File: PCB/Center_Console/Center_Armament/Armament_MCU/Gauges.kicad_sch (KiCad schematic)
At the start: 4 parts, among them U5 DRV8833PW

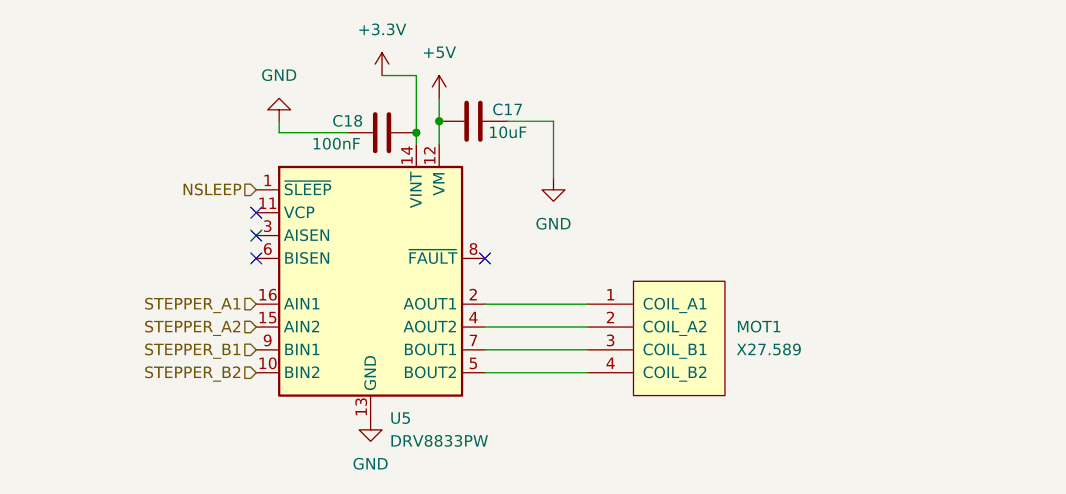
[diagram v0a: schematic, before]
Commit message: Switch stepper driver DRV8835 → DRV8833PW; rework IRLML2502 symbol
DRV8835 is only available in WSON-12 (bottom-terminated, not inspectable
post-reflow). Replaced throughout with DRV8833PW (HTSSOP-16) which is
already placed in Gauges.kicad_sch as the placeholder.

Library: remove DRV8835 symbol block from OpenSkyhawk.kicad_sym; rework
IRLML2502 symbol body with proper N-channel MOSFET graphical elements
(was a plain rectangle).

Docs: update hardware-standards.md stepper driver section (DRV8833PW,
VINT/VCP/AISEN/FAULT handling); update kicad.md library table; update
Center_Armament.md MCU board component list.

Schematics: KiCad project file and sub-sheets updated from Symbol Editor
session (IRLML2502 symbol refresh across Backlighting and Gauges sheets).
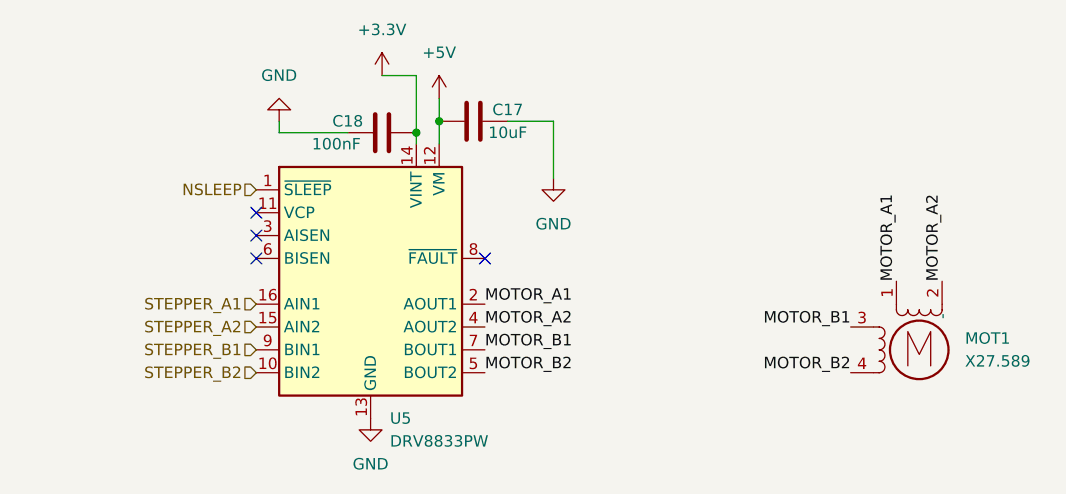
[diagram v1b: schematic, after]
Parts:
- C17, C18: footprint (none) -> Capacitor_SMD:C_0805_2012Metric
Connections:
- net MOTOR_A1: now reaches MOT1.1, U5.2 (AOUT1)
- net MOTOR_A2: now reaches MOT1.2 (-), U5.4 (AOUT2)
- net MOTOR_B1: now reaches MOT1.3, U5.7 (BOUT1)
- net MOTOR_B2: now reaches MOT1.4, U5.5 (BOUT2)
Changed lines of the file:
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@@
 	(wire
 		(pts
-			(xy 194.31 74.93) (xy 205.74 74.93)
+			(xy 196.85 54.61) (xy 201.93 54.61)
 		)
 		(stroke
@@
 	(wire
 		(pts
-			(xy 196.85 54.61) (xy 201.93 54.61)
+			(xy 186.69 57.15) (xy 186.69 55.88)
 		)
 		(stroke
@@
 	(wire
 		(pts
-			(xy 186.69 57.15) (xy 186.69 55.88)
+			(xy 189.23 52.07) (xy 189.23 54.61)
 		)
 		(stroke
@@
 	(wire
 		(pts
-			(xy 189.23 52.07) (xy 189.23 54.61)
+			(xy 186.69 49.53) (xy 186.69 55.88)
 		)
 		(stroke
@@
 	(wire
 		(pts
-			(xy 194.31 82.55) (xy 205.74 82.55)
+			(xy 201.93 54.61) (xy 201.93 60.96)
 		)
 		(stroke
@@
 	(wire
 		(pts
-			(xy 186.69 49.53) (xy 186.69 55.88)
+			(xy 189.23 54.61) (xy 189.23 57.15)
 		)
 		(stroke
@@
 	(wire
 		(pts
-			(xy 201.93 54.61) (xy 201.93 60.96)
+			(xy 171.45 55.88) (xy 179.07 55.88)
 		)
 		(stroke
@@
 	(wire
 		(pts
-			(xy 194.31 77.47) (xy 205.74 77.47)
+			(xy 186.69 49.53) (xy 182.88 49.53)
 		)
 		(stroke
@@
 	(wire
 		(pts
-			(xy 189.23 54.61) (xy 189.23 57.15)
+			(xy 171.45 54.61) (xy 171.45 55.88)
 		)
 		(stroke
@@
 		)
 	)
-	(wire
-		(pts
-			(xy 171.45 55.88) (xy 179.07 55.88)
-		)
-		(stroke
-			(width 0)
-			(type default)
-		)
-	)
-	(wire
-		(pts
-			(xy 186.69 49.53) (xy 182.88 49.53)
-		)
-		(stroke
-			(width 0)
-			(type default)
-		)
-	)
-	(wire
-		(pts
-			(xy 171.45 54.61) (xy 171.45 55.88)
-		)
-		(stroke
-			(width 0)
-			(type default)
-		)
-	)
-	(wire
-		(pts
-			(xy 194.31 80.01) (xy 205.74 80.01)
-		)
-		(stroke
-			(width 0)
-			(type default)
+	(label "MOTOR_B1"
+		(at 194.31 80.01 0)
+		(effects
+			(font
+				(size 1.27 1.27)
+			)
+			(justify left bottom)
+		)
+	)
+	(label "MOTOR_B2"
+		(at 194.31 82.55 0)
+		(effects
+			(font
+				(size 1.27 1.27)
+			)
+			(justify left bottom)
+		)
+	)
+	(label "MOTOR_B1"
+		(at 234.95 77.47 180)
+		(effects
+			(font
+				(size 1.27 1.27)
+			)
+			(justify right bottom)
+		)
+	)
+	(label "MOTOR_A1"
+		(at 194.31 74.93 0)
+		(effects
+			(font
+				(size 1.27 1.27)
+			)
+			(justify left bottom)
+		)
+	)
+	(label "MOTOR_B2"
+		(at 234.95 82.55 180)
+		(effects
+			(font
+				(size 1.27 1.27)
+			)
+			(justify right bottom)
+		)
+	)
+	(label "MOTOR_A2"
+		(at 194.31 77.47 0)
+		(effects
+			(font
+				(size 1.27 1.27)
+			)
+			(justify left bottom)
+		)
+	)
+	(label "MOTOR_A1"
+		(at 240.03 72.39 90)
+		(effects
+			(font
+				(size 1.27 1.27)
+			)
+			(justify left bottom)
+		)
+	)
+	(label "MOTOR_A2"
+		(at 245.11 72.39 90)
+		(effects
+			(font
+				(size 1.27 1.27)
+			)
+			(justify left bottom)
 		)
 	)
@@
 			)
 		)
-		(property "Footprint" ""
+		(property "Footprint" "Capacitor_SMD:C_0805_2012Metric"
 			(at 196.85 53.6448 0)
 			(hide yes)
@@
 	(symbol
 		(lib_id "OpenSkyhawk:X27.589_Stepper")
-		(at 215.9 78.74 0)
+		(at 241.3 80.01 0)
 		(unit 1)
 		(body_style 1)
@@
 		(fields_autoplaced yes)
 		(property "Reference" "MOT1"
-			(at 222.25 77.4699 0)
+			(at 247.65 78.7399 0)
 			(show_name no)
 			(do_not_autoplace no)
@@
 		)
 		(property "Value" "X27.589"
-			(at 222.25 80.0099 0)
+			(at 247.65 81.2799 0)
 			(show_name no)
 			(do_not_autoplace no)
@@
 		)
 		(property "Footprint" "OpenSkyhawk:X27.589_Stepper"
-			(at 215.9 78.74 0)
-			(hide yes)
-			(show_name no)
-			(do_not_autoplace no)
-			(effects
-				(font
-					(size 1.27 1.27)
-				)
-			)
-		)
-		(property "Datasheet" "https://www.juken-swiss.com/en/products/switec-instruments/"
-			(at 215.9 78.74 0)
+			(at 241.3 80.01 0)
+			(hide yes)
+			(show_name no)
+			(do_not_autoplace no)
+			(effects
+				(font
+					(size 1.27 1.27)
+				)
+			)
+		)
+		(property "Datasheet" "http://agr.ucoz.lv/files/SP_X27_e_C.pdf"
+			(at 241.3 80.01 0)
 			(hide yes)
 			(show_name no)
@@
 		)
 		(property "Description" "Switec X27.589 bipolar instrument stepper motor, shaft-through-PCB mount"
-			(at 215.9 78.74 0)
+			(at 241.3 80.01 0)
 			(hide yes)
 			(show_name no)
@@
 			)
 		)
-		(property "Footprint" ""
+		(property "Footprint" "Capacitor_SMD:C_0805_2012Metric"
 			(at 186.69 54.9148 0)
 			(hide yes)

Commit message: Fix DRV8833PW wiring in Gauges sheet
- VINT (pin 14): remove +3V3 connection; C18 (100nF) now bypasses VINT
  to GND only (VINT is an output, not a power input)
- VCP (pin 11): add C19 (100nF) from +5V to VCP for internal charge pump
- Add PWR_FLAG on VINT net to satisfy ERC
- Replace VM net label with +5V throughout sheet (same net, cleaner)
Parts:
- added C19: 100nF, Capacitor_SMD:C_0805_2012Metric, symbol Device:C
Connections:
- net +5V: now also C19.1
- net at U5.11 (VCP): now also C19.2
- net +3.3V: no longer names the net of C18.2, U5.14 (VINT)
- no-connect marks 4 -> 3
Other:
- moved on the sheet: C17
